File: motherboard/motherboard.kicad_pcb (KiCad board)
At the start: 2 copper layers, 29 parts, among them J1 Conn_01x02_Male, J2 Conn_01x02_Male, J3 Conn_01x02_Male, J4 Conn_01x02_Male, J5 Conn_01x02_Male, J6 XLR3, J7 Conn_01x02_Male, P1 Raspberry_Pi_+_Conn, Q1 Q_NMOS_GSD, Q2 Q_NMOS_GSD, U1 74AUC2G04, U2 4081, U3 TLC272

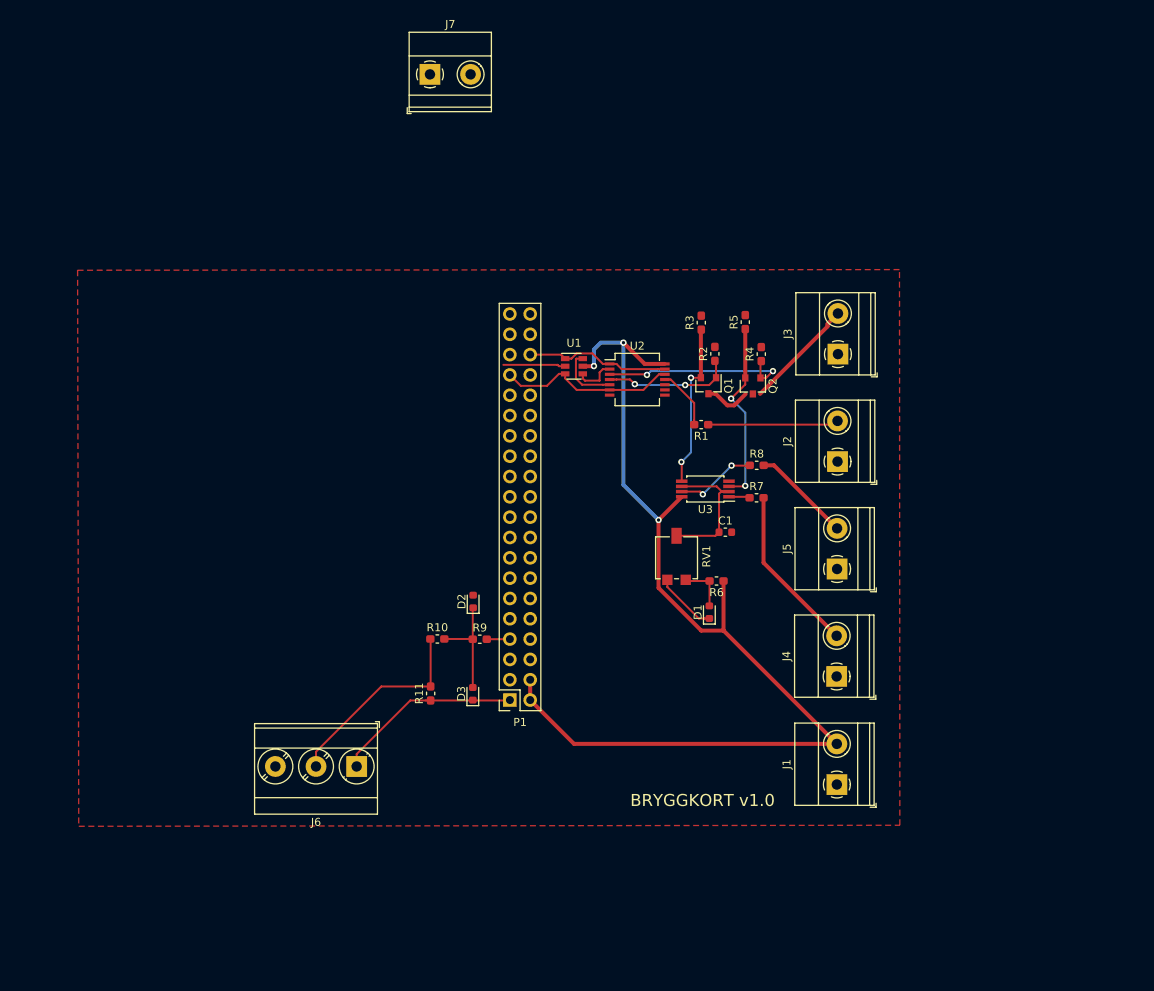
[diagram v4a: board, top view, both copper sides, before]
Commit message: Moving to RPI hat PCB
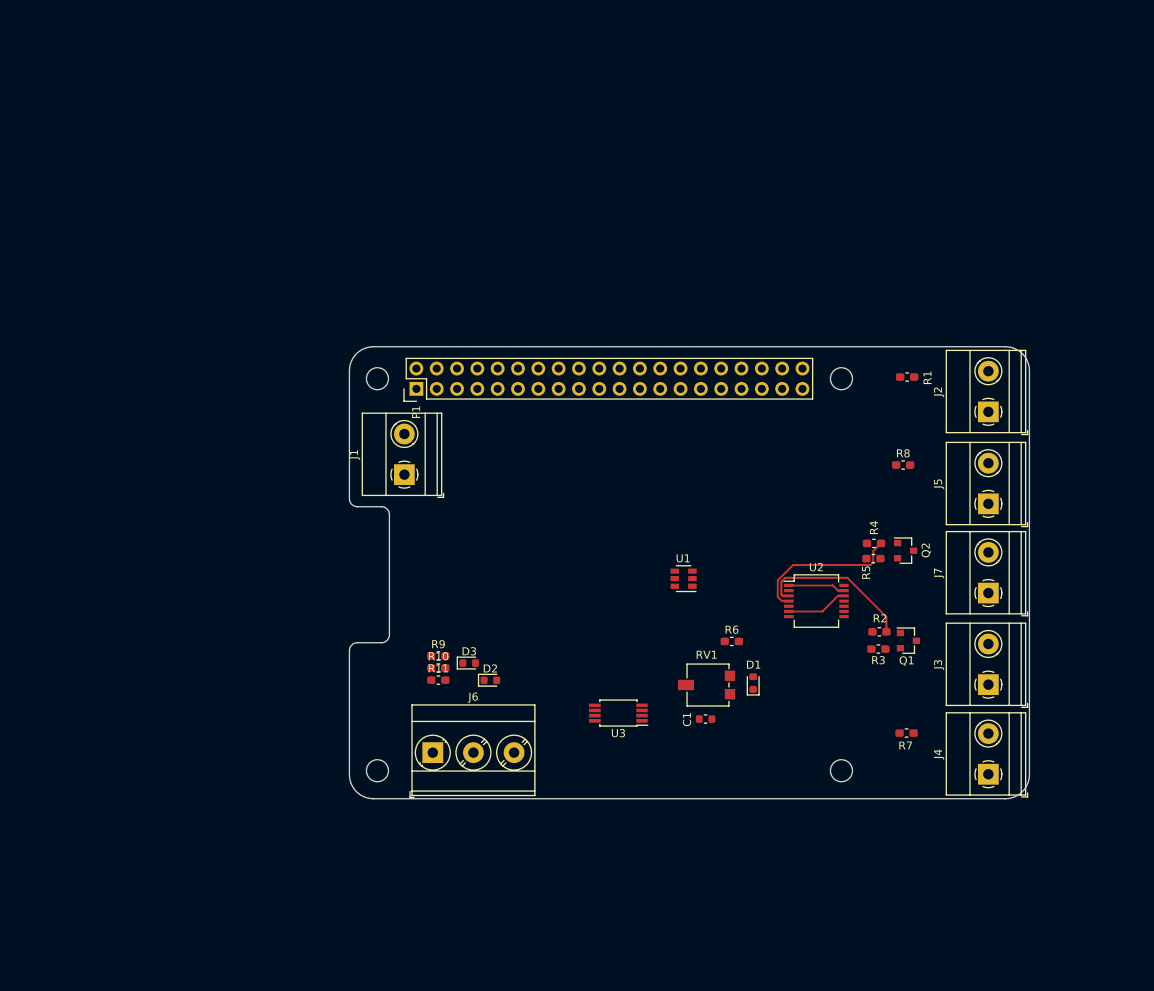
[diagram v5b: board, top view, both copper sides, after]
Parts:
- added ?: , RPi_Hat:RPi_Hat_Mounting_Hole, F.Cu at (116.7, 42.5)
- added ?: , RPi_Hat:RPi_Hat_Mounting_Hole, F.Cu at (116.7, 91.5)
- added ?: , RPi_Hat:RPi_Hat_Mounting_Hole, F.Cu at (58.7, 91.5)
- added ?: , RPi_Hat:RPi_Hat_Mounting_Hole, F.Cu at (58.7, 42.5)
- P1: footprint Connector_PinSocket_2.54mm:PinSocket_2x20_P2.54mm_Vertical -> RPi_Hat:Pin_Header_Straight_2x20
- moved J7 95.3 mm to (135.1, 69.3), turned to 90 degrees
- moved J1 66.5 mm to (62.1, 54.5)
- moved R3 46.4 mm to (121.3, 76.3), turned to 180 degrees
- moved J3 45.4 mm to (135.1, 80.8)
- moved P1 42.1 mm to (87.7, 42.5), turned to 90 degrees
- moved Q1 40.5 mm to (125.1, 75.2), turned to 0 degrees
- moved R2 40.4 mm to (121.5, 74.2), turned to 180 degrees
- moved U2 35.6 mm to (113.6, 70.3)
- moved R7 34.9 mm to (124.9, 86.8)
- moved R5 33.6 mm to (120.7, 65.0), turned to 180 degrees
- moved U3 30.0 mm to (88.8, 84.3)
- moved U1 29.9 mm to (97.0, 67.5), turned to 180 degrees
- moved Q2 28.1 mm to (124.8, 64.0), turned to 0 degrees
- moved R4 27.5 mm to (120.8, 63.1), turned to 180 degrees
- moved R1 26.4 mm to (125.0, 42.3)
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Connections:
- U2 pad 1: /SSR_interface/SSR1_GPIO -> Net-(U1-Pad6)
- U2 pad 2: Net-(U1-Pad4) -> /SSR_interface/SSR2_GPIO
- U2 pad 3: /SSR_interface/SSR_driver_2/sig_in -> /SSR_interface/SSR_driver_1/sig_in
- U2 pad 4: /SSR_interface/SSR_driver_1/sig_in -> /SSR_interface/SSR_driver_2/sig_in
- U2 pad 5: Net-(U1-Pad6) -> /SSR_interface/SSR1_GPIO
- U2 pad 6: /SSR_interface/SSR2_GPIO -> Net-(U1-Pad4)
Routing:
- net +5V: track 130.1 -> 0.00 mm, vias 3 -> 0
- net Net-(J6-Pad2): track 25.5 -> 0.00 mm
- net /SSR_interface/SSR_driver_2/indicator: track 23.8 -> 0.00 mm, vias 2 -> 0
- net /Temp_interface/+3.3V: track 23.6 -> 0.00 mm
- net Net-(J4-Pad2): track 21.6 -> 0.00 mm
- net /SSR_interface/SSR_driver_1/indicator: track 20.7 -> 0.00 mm, vias 2 -> 0
- net /SSR_interface/SSR_driver_1/ssr_in: track 19.9 -> 0.00 mm
- net Net-(C1-Pad1): track 17.8 -> 0.00 mm
- net Net-(J2-Pad2): track 16.4 -> 0.00 mm
- net GND: track 15.6 -> 0.00 mm
- net /SSR_interface/SSR2_GPIO: track 22.5 -> 7.71 mm
- net Net-(D2-Pad1): track 13.6 -> 0.00 mm
- net Net-(J5-Pad2): track 12.4 -> 0.00 mm
- net /SSR_interface/SSR1_GPIO: track 18.2 -> 7.17 mm
- net Net-(R8-Pad1): track 10.1 -> 0.00 mm, vias 2 -> 0
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- removed copper zone on F.Cu, net GND
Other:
- board outline added: 85 x 56.5 mm
- net class Default: via_dia 0.8 -> 0.6
- rule trace_min: 0.2 -> 0.01
- board text removed: "BRYGGKORT v1.0"

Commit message: Cosmetic changes
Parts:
- moved C1 5.15 mm to (94.6, 85.5), turned to 270 degrees
- moved R9 3.81 mm to (66.3, 73.4)
- moved D2 3.54 mm to (73.5, 76.7)
- moved R10 1.99 mm to (66.3, 76.7)
- moved D3 1.34 mm to (70.0, 76.7)
- moved R11 0.18 mm to (66.3, 80.0)
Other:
- board size 85 x 56.5 mm -> 82 x 56.5 mm
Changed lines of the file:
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@@
-(kicad_pcb (version 20171130) (host pcbnew 5.0.1)
+(kicad_pcb (version 20171130) (host pcbnew 5.0.2-bee76a0~70~ubuntu16.04.1)
   (general
     (thickness 1.6)
@@
   )
   (module Capacitor_SMD:C_0603_1608Metric (layer F.Cu)
-    (at 99.75 85.05)
+    (at 94.615 85.4965 270)
     (descr "Capacitor SMD 0603 (1608 Metric), square (rectangular) end terminal, IPC_7351 nominal, (Body size source: http://www.tortai-tech.com/upload/download/2011102023233369053.pdf), generated with kicad-footprint-generator")
     (tags capacitor)
     (attr smd)
-    (fp_text reference C1 (at -2.2875 0.05 270) (layer F.SilkS)
-      (effects (font (size 1 1) (thickness 0.15)))
-    )
-    (fp_text value C (at -0.7875 1.6 90) (layer F.Fab)
+    (fp_text reference C1 (at -2.54 0 180) (layer F.SilkS)
+      (effects (font (size 1 1) (thickness 0.15)))
+    )
+    (fp_text value C (at 2.54 0) (layer F.Fab)
       (effects (font (size 1 1) (thickness 0.15)))
     )
@@
     (fp_line (start 1.48 -0.73) (end 1.48 0.73) (layer F.CrtYd) (width 0.05))
     (fp_line (start 1.48 0.73) (end -1.48 0.73) (layer F.CrtYd) (width 0.05))
-    (fp_text user %R (at 0 0) (layer F.Fab)
+    (fp_text user %R (at 0 0 270) (layer F.Fab)
       (effects (font (size 0.4 0.4) (thickness 0.06)))
     )
-    (pad 1 smd roundrect (at -0.7875 0) (size 0.875 0.95) (layers F.Cu F.Paste F.Mask) (roundrect_rratio 0.25)
+    (pad 1 smd roundrect (at -0.7875 0 270) (size 0.875 0.95) (layers F.Cu F.Paste F.Mask) (roundrect_rratio 0.25)
       (net 2 "Net-(C1-Pad1)"))
-    (pad 2 smd roundrect (at 0.7875 0) (size 0.875 0.95) (layers F.Cu F.Paste F.Mask) (roundrect_rratio 0.25)
+    (pad 2 smd roundrect (at 0.7875 0 270) (size 0.875 0.95) (layers F.Cu F.Paste F.Mask) (roundrect_rratio 0.25)
       (net 3 GND))
     (model ${KISYS3DMOD}/Capacitor_SMD.3dshapes/C_0603_1608Metric.wrl
@@
   )
   (module Diode_SMD:D_0603_1608Metric (layer F.Cu)
-    (at 72.85 80.2)
+    (at 73.5075 76.7225)
     (descr "Diode SMD 0603 (1608 Metric), square (rectangular) end terminal, IPC_7351 nominal, (Body size source: http://www.tortai-tech.com/upload/download/2011102023233369053.pdf), generated with kicad-footprint-generator")
     (tags diode)
@@
   )
   (module Diode_SMD:D_0603_1608Metric (layer F.Cu)
-    (at 70.2 78.05)
+    (at 70.01125 76.7225)
     (descr "Diode SMD 0603 (1608 Metric), square (rectangular) end terminal, IPC_7351 nominal, (Body size source: http://www.tortai-tech.com/upload/download/2011102023233369053.pdf), generated with kicad-footprint-generator")
     (tags diode)
@@
   )
   (module Resistor_SMD:R_0603_1608Metric_Pad1.05x0.95mm_HandSolder (layer F.Cu)
-    (at 66.345001 77.165001)
+    (at 66.345001 73.355001)
     (descr "Resistor SMD 0603 (1608 Metric), square (rectangular) end terminal, IPC_7351 nominal with elongated pad for handsoldering. (Body size source: http://www.tortai-tech.com/upload/download/2011102023233369053.pdf), generated with kicad-footprint-generator")
     (tags "resistor handsolder")
@@
   )
   (module Resistor_SMD:R_0603_1608Metric_Pad1.05x0.95mm_HandSolder (layer F.Cu)
-    (at 66.345001 78.675001)
+    (at 66.345001 76.6825)
     (descr "Resistor SMD 0603 (1608 Metric), square (rectangular) end terminal, IPC_7351 nominal with elongated pad for handsoldering. (Body size source: http://www.tortai-tech.com/upload/download/2011102023233369053.pdf), generated with kicad-footprint-generator")
     (tags "resistor handsolder")
@@
   )
   (module Resistor_SMD:R_0603_1608Metric_Pad1.05x0.95mm_HandSolder (layer F.Cu)
-    (at 66.345001 80.185001)
+    (at 66.345001 80.01)
     (descr "Resistor SMD 0603 (1608 Metric), square (rectangular) end terminal, IPC_7351 nominal with elongated pad for handsoldering. (Body size source: http://www.tortai-tech.com/upload/download/2011102023233369053.pdf), generated with kicad-footprint-generator")
     (tags "resistor handsolder")
@@
     (tags "SSOP 0.65")
     (attr smd)
-    (fp_text reference U3 (at 0 -2.55 180) (layer F.SilkS)
-      (effects (font (size 1 1) (thickness 0.15)))
-    )
-    (fp_text value TLC272 (at 0 2.55 180) (layer F.Fab)
+    (fp_text reference U3 (at -0.05 2.385 180) (layer F.SilkS)
+      (effects (font (size 1 1) (thickness 0.15)))
+    )
+    (fp_text value TLC272 (at -0.05 -2.695 180) (layer F.Fab)
       (effects (font (size 1 1) (thickness 0.15)))
     )
@@
   )
   (dimension 17 (width 0.15) (layer Dwgs.User)
-    (gr_text "17 mm" (at 64.58 67.01 270) (layer Dwgs.User)
+    (gr_text "17 mm" (at 64.58 63.2 270) (layer Dwgs.User)
       (effects (font (size 1.5 1.5) (thickness 0.15)))
     )
-    (feature1 (pts (xy 61.23 75.51) (xy 65.93 75.51)))
-    (feature2 (pts (xy 61.23 58.51) (xy 65.93 58.51)))
-    (crossbar (pts (xy 63.23 58.51) (xy 63.23 75.51)))
-    (arrow1a (pts (xy 63.23 75.51) (xy 62.643579 74.383496)))
-    (arrow1b (pts (xy 63.23 75.51) (xy 63.816421 74.383496)))
-    (arrow2a (pts (xy 63.23 58.51) (xy 62.643579 59.636504)))
-    (arrow2b (pts (xy 63.23 58.51) (xy 63.816421 59.636504)))
+    (feature1 (pts (xy 61.23 71.7) (xy 65.93 71.7)))
+    (feature2 (pts (xy 61.23 54.7) (xy 65.93 54.7)))
+    (crossbar (pts (xy 63.23 54.7) (xy 63.23 71.7)))
+    (arrow1a (pts (xy 63.23 71.7) (xy 62.643579 70.573496)))
+    (arrow1b (pts (xy 63.23 71.7) (xy 63.816421 70.573496)))
+    (arrow2a (pts (xy 63.23 54.7) (xy 62.643579 55.826504)))
+    (arrow2b (pts (xy 63.23 54.7) (xy 63.816421 55.826504)))
   )
   (dimension 5 (width 0.15) (layer Dwgs.User)
@@
   (gr_arc (start 59.23 59.51) (end 59.23 58.51) (angle 90) (layer Edge.Cuts) (width 0.1))
   (gr_arc (start 56.23 57.51) (end 56.23 58.51) (angle 90) (layer Edge.Cuts) (width 0.1))
-  (gr_arc (start 137.23 92.01) (end 140.23 92.01) (angle 90) (layer Edge.Cuts) (width 0.1))
+  (gr_arc (start 129.415 92.01) (end 132.415 92.01) (angle 90) (layer Edge.Cuts) (width 0.1))
   (gr_arc (start 58.23 92.01) (end 58.23 95.01) (angle 90) (layer Edge.Cuts) (width 0.1))
   (gr_arc (start 58.23 41.51) (end 55.23 41.51) (angle 90) (layer Edge.Cuts) (width 0.1))
-  (gr_arc (start 137.23 41.51) (end 137.23 38.51) (angle 90) (layer Edge.Cuts) (width 0.1))
+  (gr_arc (start 129.415 41.51) (end 129.415 38.51) (angle 90) (layer Edge.Cuts) (width 0.1))
   (gr_line (start 55.23 76.51) (end 55.23 92.01) (layer Edge.Cuts) (width 0.1))
   (gr_line (start 55.23 41.51) (end 55.23 57.51) (layer Edge.Cuts) (width 0.1))
@@
   (gr_line (start 60.23 59.51) (end 60.23 74.51) (layer Edge.Cuts) (width 0.1))
   (gr_line (start 58.23 95.01) (end 137.23 95.01) (angle 90) (layer Edge.Cuts) (width 0.1))
-  (gr_line (start 140.23 41.51) (end 140.23 92.01) (angle 90) (layer Edge.Cuts) (width 0.1))
+  (gr_line (start 129.415 41.51) (end 129.415 92.01) (angle 90) (layer Edge.Cuts) (width 0.1))
   (gr_line (start 58.23 38.51) (end 137.23 38.51) (angle 90) (layer Edge.Cuts) (width 0.1))
   (segment (start 114.364998 71.6) (end 116.314998 69.65) (width 0.25) (layer F.Cu) (net 14))

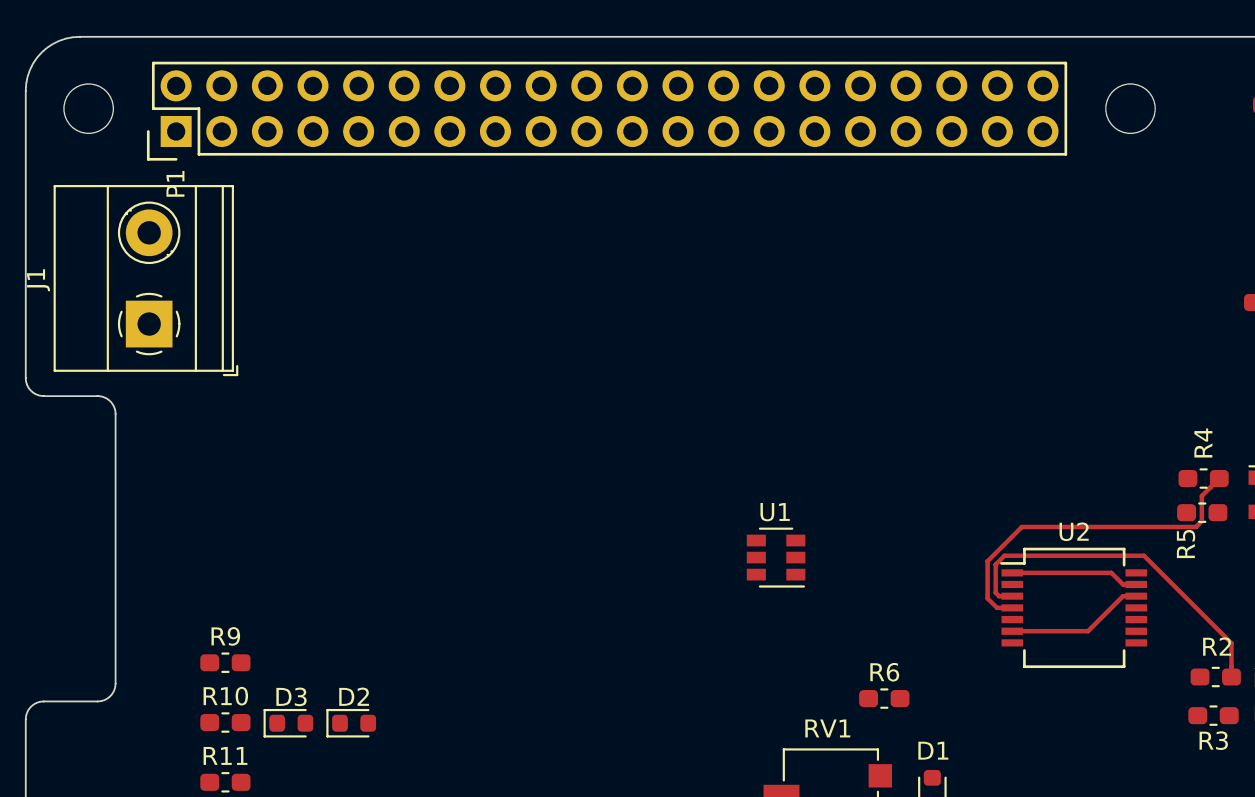
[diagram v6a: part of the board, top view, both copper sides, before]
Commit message: Fixed dual and
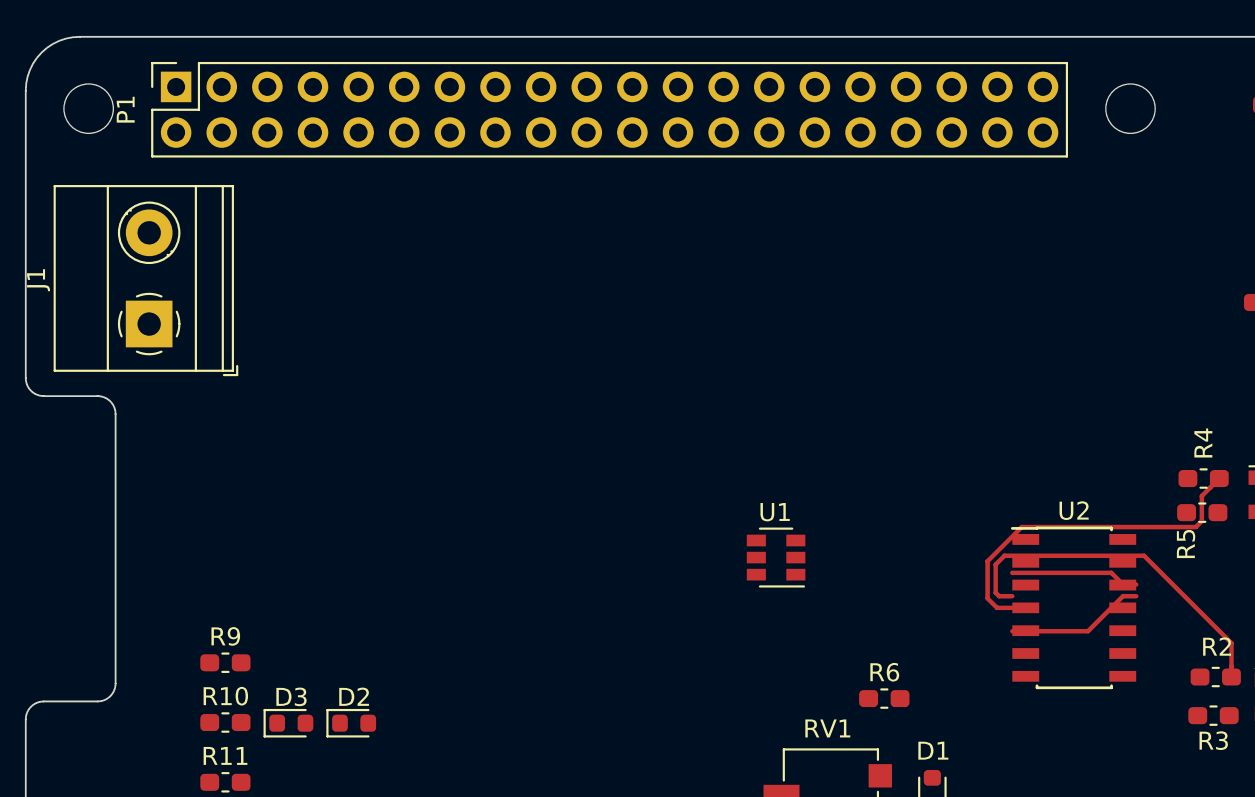
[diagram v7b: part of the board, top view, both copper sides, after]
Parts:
- P1: footprint RPi_Hat:Pin_Header_Straight_2x20 -> Connector_PinSocket_2.54mm:PinSocket_2x20_P2.54mm_Vertical
- U2: footprint Package_SO:SSOP-14_5.3x6.2mm_P0.65mm -> Package_SO:SOIC-14_3.9x8.7mm_P1.27mm
- moved P1 24.2 mm to (63.6, 41.3)
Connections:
- P1 pad 10: (no net) -> Net-(P1-Pad10)
- P1 pad 11: (no net) -> Net-(P1-Pad11)
- P1 pad 12: (no net) -> Net-(P1-Pad12)
- P1 pad 13: (no net) -> Net-(P1-Pad13)
- P1 pad 14: (no net) -> Net-(P1-Pad14)
- P1 pad 15: (no net) -> Net-(P1-Pad15)
- P1 pad 16: (no net) -> Net-(P1-Pad16)
- P1 pad 17: (no net) -> Net-(P1-Pad17)
- P1 pad 18: (no net) -> Net-(P1-Pad18)
- P1 pad 19: (no net) -> Net-(P1-Pad19)
- P1 pad 21: (no net) -> Net-(P1-Pad21)
- P1 pad 22: (no net) -> Net-(P1-Pad22)
- P1 pad 23: (no net) -> Net-(P1-Pad23)
- P1 pad 24: (no net) -> Net-(P1-Pad24)
- P1 pad 25: (no net) -> Net-(P1-Pad25)
- P1 pad 26: (no net) -> Net-(P1-Pad26)
- P1 pad 27: (no net) -> Net-(P1-Pad27)
- P1 pad 28: (no net) -> Net-(P1-Pad28)
- P1 pad 29: (no net) -> Net-(P1-Pad29)
- P1 pad 3: (no net) -> Net-(P1-Pad3)
- P1 pad 30: (no net) -> Net-(P1-Pad30)
- P1 pad 31: (no net) -> Net-(P1-Pad31)
- P1 pad 32: (no net) -> Net-(P1-Pad32)
- P1 pad 34: (no net) -> Net-(P1-Pad34)
- P1 pad 35: (no net) -> Net-(P1-Pad35)
- P1 pad 37: (no net) -> Net-(P1-Pad37)
- P1 pad 38: (no net) -> Net-(P1-Pad38)
- P1 pad 39: (no net) -> Net-(P1-Pad39)
- P1 pad 40: (no net) -> Net-(P1-Pad40)
- P1 pad 5: (no net) -> Net-(P1-Pad5)
- P1 pad 6: (no net) -> Net-(P1-Pad6)
- P1 pad 8: (no net) -> Net-(P1-Pad8)
- P1 pad 9: (no net) -> Net-(P1-Pad9)
- U2 pad 10: (no net) -> Net-(U2-Pad10)
- U2 pad 8: (no net) -> Net-(U2-Pad8)
- U2 pad 9: (no net) -> Net-(U2-Pad9)
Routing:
- net /SSR_interface/SSR2_GPIO: track 7.71 -> 7.17 mm
- net /SSR_interface/SSR1_GPIO: track 7.17 -> 7.71 mm

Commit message: Logo
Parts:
- added G***: LOGO, graphic:bryggans_logo, F.Cu at (86.2, 59.6)
- moved U3 10.2 mm to (97.3, 78.7), turned to 270 degrees
- moved U1 10.1 mm to (105.5, 73.0), turned to 270 degrees
- moved C1 6.08 mm to (97.2, 91.0)
- moved RV1 6.08 mm to (102.7, 86.3)
- moved D1 6.08 mm to (108.3, 86.0)
- moved R6 6.08 mm to (105.6, 80.8)
- moved R5 0.78 mm to (121.5, 65.1)
- moved R4 0.70 mm to (121.5, 63.0)
- moved R8 0.50 mm to (125.0, 53.3)
- moved Q2 0.35 mm to (125.1, 64.0)
- moved R3 0.16 mm to (121.5, 76.2)
- moved R7 0.08 mm to (125.0, 86.8)
- moved R2 0.06 mm to (121.5, 74.2)
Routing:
- net /SSR_interface/SSR_driver_1/sig_in: track 19.8 -> 0.00 mm
- net /SSR_interface/SSR_driver_2/sig_in: track 19.3 -> 0.00 mm
- net /SSR_interface/SSR1_GPIO: track 7.71 -> 0.00 mm
- net /SSR_interface/SSR2_GPIO: track 7.17 -> 6.66 mm
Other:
- board size 82 x 56.5 mm -> 85 x 56.5 mm
